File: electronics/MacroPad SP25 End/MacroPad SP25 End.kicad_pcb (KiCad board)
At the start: 2 copper layers, 14 parts, among them J1 Conn_01x07_Pin, J2 Conn_01x07_Pin, J3 Conn_01x07_Pin, J4 Conn_01x07_Pin, SW1 RotaryEncoder_Switch, SW2 RotaryEncoder_Switch

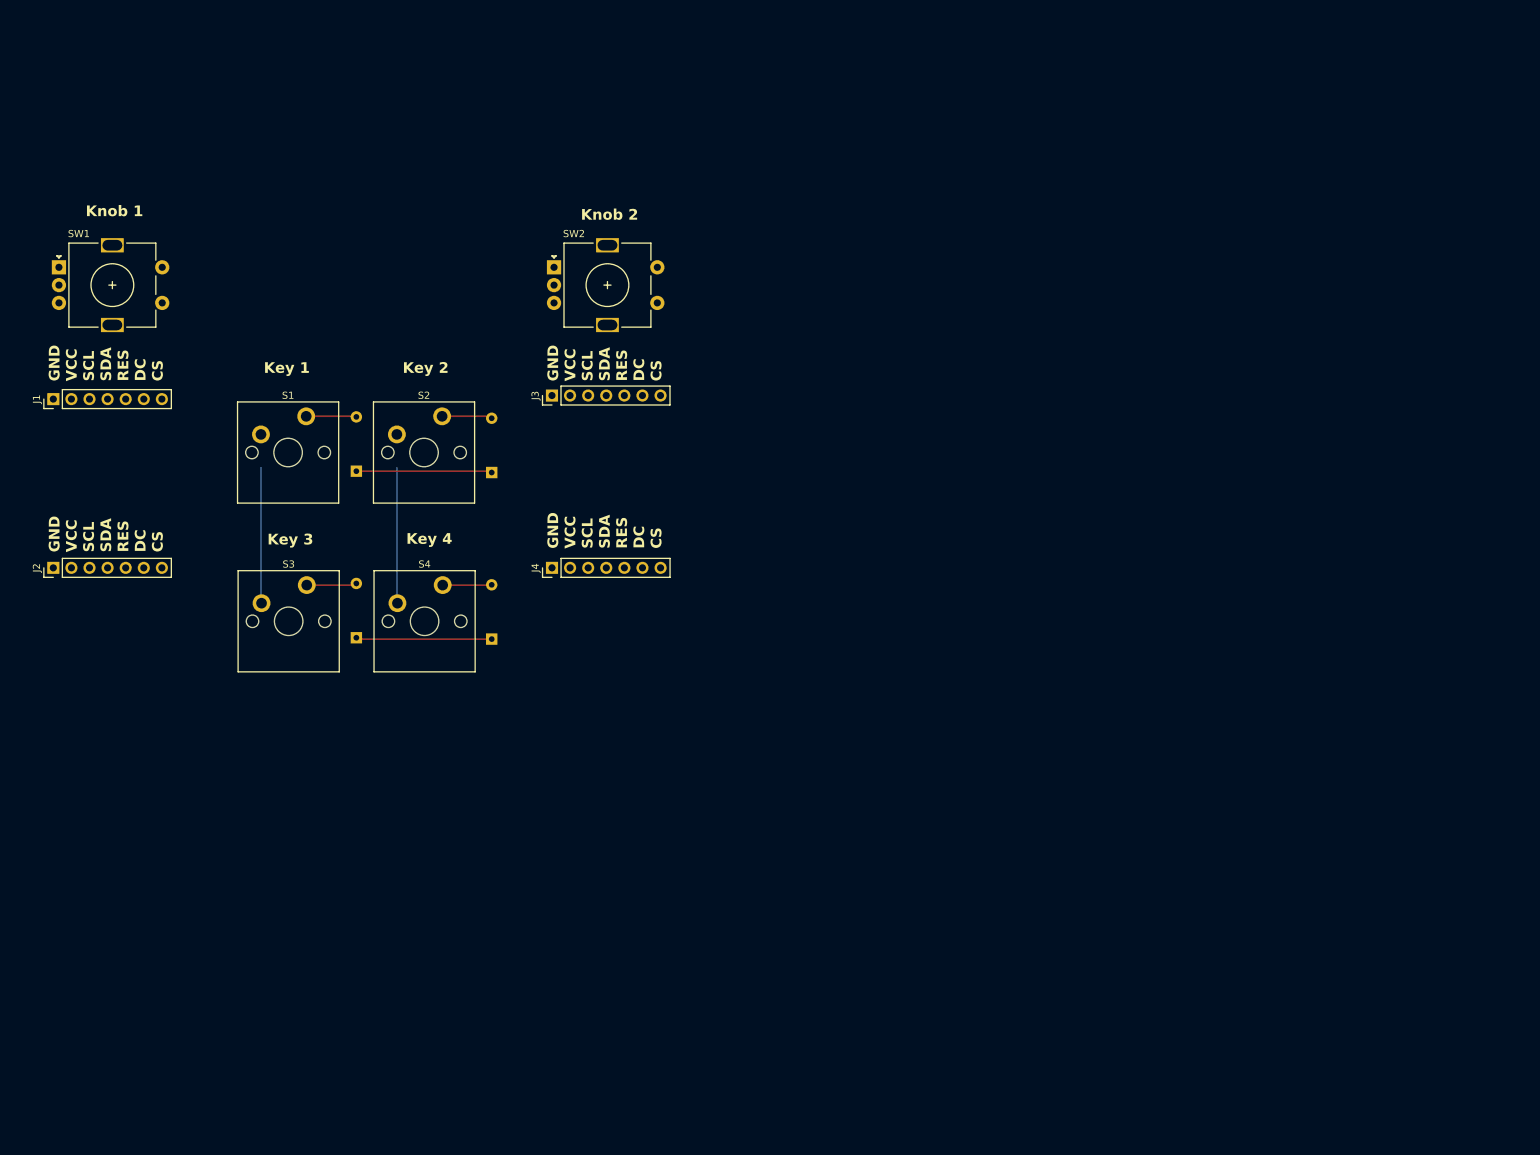
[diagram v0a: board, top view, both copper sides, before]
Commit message: updated sp25 end -- wiring to esp and routing left
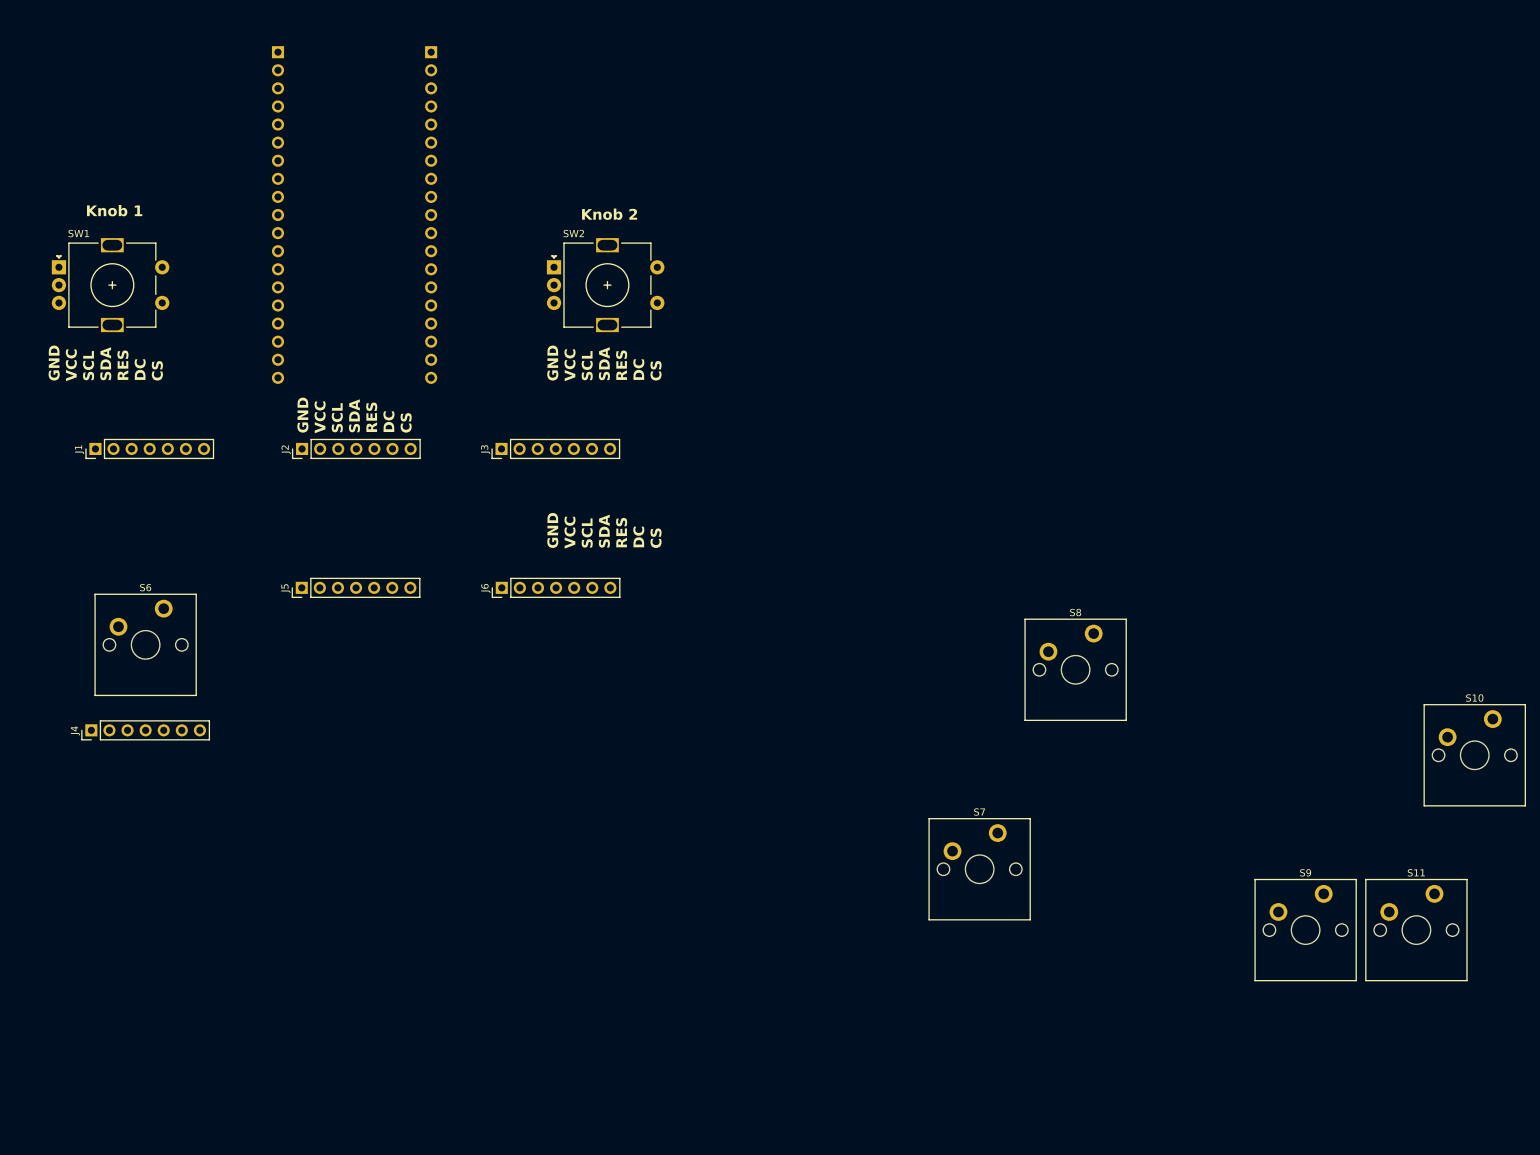
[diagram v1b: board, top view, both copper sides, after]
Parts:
- removed D1, D2, D4, D5: Diode, ScottoKeebs_Components:Diode_DO-35
- removed S1, S2, S3, S4: Keyswitch, ScottoKeebs_MX:MX_PCB_1.00u
- added J5: Conn_01x07_Pin, Connector_PinHeader_2.54mm:PinHeader_1x07_P2.54mm_Vertical, F.Cu at (111.3, 97.5)
- added J6: Conn_01x07_Pin, Connector_PinHeader_2.54mm:PinHeader_1x07_P2.54mm_Vertical, F.Cu at (139.4, 97.5)
- added J7: Conn_01x19_MountingPin, Connector_PinHeader_2.54mm:PinHeader_1x19_P2.54mm_Vertical, B.Cu at (129.5, 22.3)
- added J8: Conn_01x19_MountingPin, Connector_PinHeader_2.54mm:PinHeader_1x19_P2.54mm_Vertical, B.Cu at (108.0, 22.3)
- added S10: Keyswitch, ScottoKeebs_MX:MX_PCB_1.00u, F.Cu at (276.0, 121.0)
- added S11: Keyswitch, ScottoKeebs_MX:MX_PCB_1.00u, F.Cu at (267.8, 145.5)
- added S6: Keyswitch, ScottoKeebs_MX:MX_PCB_1.00u, F.Cu at (89.4, 105.5)
- added S7: Keyswitch, ScottoKeebs_MX:MX_PCB_1.00u, F.Cu at (206.5, 137.0)
- added S8: Keyswitch, ScottoKeebs_MX:MX_PCB_1.00u, F.Cu at (220.0, 109.0)
- added S9: Keyswitch, ScottoKeebs_MX:MX_PCB_1.00u, F.Cu at (252.3, 145.5)
- moved J4 68.6 mm to (81.8, 117.5)
- moved J2 38.7 mm to (111.4, 78.0)
- moved J3 10.3 mm to (139.4, 78.0)
- moved J1 9.16 mm to (82.4, 78.0)
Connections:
- J1 pad 1: unconnected-(J1-Pin_1-Pad1) -> GND
- J1 pad 2: unconnected-(J1-Pin_2-Pad2) -> VCC
- J1 pad 3: unconnected-(J1-Pin_3-Pad3) -> SCL
- J1 pad 4: unconnected-(J1-Pin_4-Pad4) -> SDA
- J1 pad 5: unconnected-(J1-Pin_5-Pad5) -> RES
- J1 pad 6: unconnected-(J1-Pin_6-Pad6) -> DC
- J1 pad 7: unconnected-(J1-Pin_7-Pad7) -> CS1
- J2 pad 1: unconnected-(J2-Pin_1-Pad1) -> GND
- J2 pad 2: unconnected-(J2-Pin_2-Pad2) -> VCC
- J2 pad 3: unconnected-(J2-Pin_3-Pad3) -> SCL
- J2 pad 4: unconnected-(J2-Pin_4-Pad4) -> SDA
- J2 pad 5: unconnected-(J2-Pin_5-Pad5) -> RES
- J2 pad 6: unconnected-(J2-Pin_6-Pad6) -> DC
- J2 pad 7: unconnected-(J2-Pin_7-Pad7) -> CS2
- J3 pad 1: unconnected-(J3-Pin_1-Pad1) -> GND
- J3 pad 2: unconnected-(J3-Pin_2-Pad2) -> VCC
- J3 pad 3: unconnected-(J3-Pin_3-Pad3) -> SCL
- J3 pad 4: unconnected-(J3-Pin_4-Pad4) -> SDA
- J3 pad 5: unconnected-(J3-Pin_5-Pad5) -> RES
- J3 pad 6: unconnected-(J3-Pin_6-Pad6) -> DC
- J3 pad 7: unconnected-(J3-Pin_7-Pad7) -> CS3
- J4 pad 1: unconnected-(J4-Pin_1-Pad1) -> GND
- J4 pad 2: unconnected-(J4-Pin_2-Pad2) -> VCC
- J4 pad 3: unconnected-(J4-Pin_3-Pad3) -> SCL
- J4 pad 4: unconnected-(J4-Pin_4-Pad4) -> SDA
- J4 pad 5: unconnected-(J4-Pin_5-Pad5) -> RES
- J4 pad 6: unconnected-(J4-Pin_6-Pad6) -> DC
- J4 pad 7: unconnected-(J4-Pin_7-Pad7) -> CS4
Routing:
- net Row 1: track 19.1 -> 0.00 mm
- net Row 0: track 19.1 -> 0.00 mm
- net Col 1: track 19.0 -> 0.00 mm
- net Col 0: track 19.0 -> 0.00 mm
- net Net-(D1-A): track 7.07 -> 0.00 mm
- net Net-(D2-A): track 7.07 -> 0.00 mm
- net Net-(D4-A): track 7.06 -> 0.00 mm
- net Net-(D5-A): track 6.90 -> 0.00 mm
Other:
- board text removed: "Key 1"
- board text removed: "Key 2"
- board text removed: "Key 3"
- board text removed: "Key 4"

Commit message: not much left
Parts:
- moved S3 158.6 mm to (113.9, 107.0)
- moved S6 143.1 mm to (133.0, 126.0)
- moved S5 139.7 mm to (114.0, 126.1)
- moved S2 88.3 mm to (133.0, 88.0)
- moved S4 87.0 mm to (133.0, 107.0)
- moved J4 68.0 mm to (146.7, 97.0)
- moved J3 58.1 mm to (84.8, 98.0)
- moved J2 35.5 mm to (146.8, 78.0)
- moved J5 32.6 mm to (84.8, 116.5)
- moved J8 30.5 mm to (138.5, 23.1)
- moved S1 30.2 mm to (114.0, 88.0)
- moved J7 21.5 mm to (108.0, 23.1)
- moved J6 19.9 mm to (146.7, 116.0)
- moved SW1 11.2 mm to (85.5, 60.1)
- moved SW2 7.50 mm to (147.0, 60.0)
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- renumbered S6 to S1, S7 to S2, S11 to S3, S8 to S4, S9 to S5, S10 to S6
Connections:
- J7 pad 10: unconnected-(J7-Pin_10-Pad10) -> Push2
- J7 pad 11: unconnected-(J7-Pin_11-Pad11) -> Up2
- J7 pad 12: unconnected-(J7-Pin_12-Pad12) -> CS4
- J7 pad 13: unconnected-(J7-Pin_13-Pad13) -> CS3
- J7 pad 14: unconnected-(J7-Pin_14-Pad14) -> Key3
- J7 pad 15: unconnected-(J7-Pin_15-Pad15) -> Key6
- J7 pad 16: unconnected-(J7-Pin_16-Pad16) -> Key5
- J7 pad 17: unconnected-(J7-Pin_17-Pad17) -> Key4
- J7 pad 19: unconnected-(J7-Pin_19-Pad19) -> VCC
- J7 pad 7: unconnected-(J7-Pin_7-Pad7) -> Key1
- J7 pad 8: unconnected-(J7-Pin_8-Pad8) -> CS6
- J7 pad 9: unconnected-(J7-Pin_9-Pad9) -> CS5
- J8 pad 10: unconnected-(J8-Pin_10-Pad10) -> CS2
- J8 pad 11: unconnected-(J8-Pin_11-Pad11) -> SCL
- J8 pad 12: unconnected-(J8-Pin_12-Pad12) -> Key2
- J8 pad 14: unconnected-(J8-Pin_14-Pad14) -> Push1
- J8 pad 17: unconnected-(J8-Pin_17-Pad17) -> Down1
- J8 pad 18: unconnected-(J8-Pin_18-Pad18) -> SDA
- J8 pad 19: unconnected-(J8-Pin_19-Pad19) -> GND
- J8 pad 4: unconnected-(J8-Pin_4-Pad4) -> CS1
- J8 pad 5: unconnected-(J8-Pin_5-Pad5) -> DC
- J8 pad 7: unconnected-(J8-Pin_7-Pad7) -> RES
- J8 pad 8: unconnected-(J8-Pin_8-Pad8) -> Down2
- J8 pad 9: unconnected-(J8-Pin_9-Pad9) -> Up1
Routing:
- net GND: track 0.00 -> 241.8 mm
- net DC: track 0.00 -> 221.4 mm
- net RES: track 0.00 -> 202.9 mm
- net SCL: track 0.00 -> 178.0 mm, vias 0 -> 3
- net SDA: track 0.00 -> 149.8 mm, vias 0 -> 2
- net VCC: track 0.00 -> 149.8 mm
- net Key6: track 0.00 -> 134.9 mm, vias 0 -> 1
- net CS4: track 0.00 -> 117.9 mm
- net CS6: track 0.00 -> 110.8 mm
- net Key5: track 0.00 -> 101.2 mm, vias 0 -> 1
- net CS1: track 0.00 -> 96.2 mm
- net CS5: track 0.00 -> 90.9 mm
- net CS3: track 0.00 -> 64.7 mm
- net Key4: track 0.00 -> 56.9 mm, vias 0 -> 4
- net Key3: track 0.00 -> 52.5 mm, vias 0 -> 4
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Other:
- board outline added: 105 x 124 mm

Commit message: new sp25 ewnd
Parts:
- moved S4 68.7 mm to (101.5, 168.0)
- moved J4 66.4 mm to (94.4, 138.0)
- moved J3 53.7 mm to (138.3, 93.0)
- moved S6 43.9 mm to (145.9, 168.0)
- moved S5 43.1 mm to (124.0, 168.0)
- moved J5 38.2 mm to (116.4, 138.0)
- moved S1 37.9 mm to (102.0, 124.0)
- moved S2 37.1 mm to (124.0, 124.0)
- moved S3 36.3 mm to (146.0, 124.1)
- moved J2 34.0 mm to (116.4, 93.0)
- moved J6 23.5 mm to (138.3, 138.0)
- moved J7 21.5 mm to (116.5, 42.8)
- moved J8 20.9 mm to (131.5, 42.8)
- moved SW1 20.1 mm to (94.8, 78.0)
- moved SW2 19.8 mm to (138.8, 78.0)
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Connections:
- SW2 pad S2: Push1 -> Push2
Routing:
- net GND: track 241.8 -> 0.00 mm
- net DC: track 221.4 -> 0.00 mm
- net RES: track 202.9 -> 0.00 mm
- net SCL: track 178.0 -> 0.00 mm, vias 3 -> 0
- net SDA: track 149.8 -> 0.00 mm, vias 2 -> 0
- net VCC: track 149.8 -> 0.00 mm
- net Key6: track 134.9 -> 0.00 mm, vias 1 -> 0
- net CS4: track 117.9 -> 0.00 mm
- net CS6: track 110.8 -> 0.00 mm
- net Key5: track 101.2 -> 0.00 mm, vias 1 -> 0
- net CS1: track 96.2 -> 0.00 mm
- net CS5: track 90.9 -> 0.00 mm
- net CS3: track 64.7 -> 0.00 mm
- net Key4: track 56.9 -> 0.00 mm, vias 4 -> 0
- net Key3: track 52.5 -> 0.00 mm, vias 4 -> 0
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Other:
- board outline removed
- board text removed: "GND VCC SCL SDA RES DC CS"
- board text removed: "Knob 1"
- board text removed: "Knob 2"
